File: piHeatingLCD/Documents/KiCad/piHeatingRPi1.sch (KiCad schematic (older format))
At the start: 17 parts, among them J1 Raspberry_Pi_1_all_pin_ordered, J2 10-pin_header_LCD_interface, J3 3-pin_KY-019_relay_header, J4 3_pin_Dallas_1-wire_connector, J5 2-pin_NO_switch_header, J6 2-pin_NO_switch_header, J7 2-pin_NO_switch_header, J8 2-pin_NO_switch_header

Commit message: updated kicad
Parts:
- added D1: LED, My_Misc:CP_Radial_D5.0mm_P2.50mm_larger_pads, symbol Device:LED
- added R10: R, My_Misc:R_Axial_DIN0207_L6.3mm_D2.5mm_P10.16mm_Horizontal_larger_pads, symbol Device:R
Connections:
- net at J1.8 (GPIO14/TXD), R1.2: now also J4.2 (DQ); no longer J3.1 (S)
- net at J1.1 (3V3), J2.9 (LED+), J5.1 (+)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: no longer J3.2 (Vcc), R1.1
- net at J1.25 (GND), J2.1 (VSS), J3.3 (GND)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: now also R10.2
- net at J1.10 (GPIO15/RXD): now also J3.1 (S), D1.2 (A); no longer J4.2 (DQ)
- net at J1.2 (5V), J2.2 (VDD), J4.3 (Vdd): now also J3.2 (Vcc), R1.1
- new net: D1.1 (K), R10.1
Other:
- moved on the sheet: J3, J4, R1
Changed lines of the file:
@@
 L My_Headers:3-pin_KY-019_relay_header J3
 U 1 1 5E585F50
-P 9800 2250
-F 0 "J3" H 9969 2265 50  0000 L CNN
-F 1 "3-pin_KY-019_relay_header" H 9800 2050 50  0001 C CNN
-F 2 "My_Headers:3-pin_KY-019_Relay_header_larger_pads" H 9800 2250 50  0001 C CNN
-F 3 "~" H 9800 2250 50  0001 C CNN
-	1    9800 2250
+P 9750 2550
+F 0 "J3" H 9919 2565 50  0000 L CNN
+F 1 "3-pin_KY-019_relay_header" H 9750 2350 50  0000 C CNN
+F 2 "My_Headers:3-pin_KY-019_Relay_header_larger_pads" H 9750 2550 50  0001 C CNN
+F 3 "~" H 9750 2550 50  0001 C CNN
+	1    9750 2550
 	1    0    0    -1
 $EndComp
@@
 L My_Headers:3_pin_Dallas_1-wire_connector J4
 U 1 1 5E58672E
-P 9800 2650
-F 0 "J4" H 9969 2665 50  0000 L CNN
-F 1 "3_pin_Dallas_1-wire_connector" H 9800 2450 50  0001 C CNN
-F 2 "My_Headers:3_pin_Dallas_1-wire_header_larger_pads" H 9800 2650 50  0001 C CNN
-F 3 "~" H 9800 2650 50  0001 C CNN
-	1    9800 2650
-	1    0    0    -1
-$EndComp
-$Comp
-L Device:R R1
-U 1 1 5E5AAFEA
-P 9000 2150
-F 0 "R1" H 9070 2196 50  0000 L CNN
-F 1 "4.7k" H 9070 2105 50  0000 L CNN
-F 2 "My_Misc:R_Axial_DIN0207_L6.3mm_D2.5mm_P10.16mm_Horizontal_larger_pads" V 8930 2150 50  0001 C CNN
-F 3 "~" H 9000 2150 50  0001 C CNN
-	1    9000 2150
-	0    -1   -1   0
+P 9750 2050
+F 0 "J4" H 9919 2065 50  0000 L CNN
+F 1 "3_pin_Dallas_1-wire_connector" H 9750 1850 50  0000 C CNN
+F 2 "My_Headers:3_pin_Dallas_1-wire_header_larger_pads" H 9750 2050 50  0001 C CNN
+F 3 "~" H 9750 2050 50  0001 C CNN
+	1    9750 2050
+	1    0    0    -1
 $EndComp
 $Comp
@@
 Connection ~ 8300 2250
 Wire Wire Line
-	9600 2550 9450 2550
-Wire Wire Line
-	8300 2750 8300 2250
-Wire Wire Line
-	8300 2750 9600 2750
-Wire Wire Line
 	9050 3350 8850 3350
 Wire Wire Line
@@
 Connection ~ 10450 3550
 Wire Wire Line
-	9450 2550 9450 2900
-Wire Wire Line
 	10450 2900 10450 3250
 Connection ~ 10450 3250
 Wire Wire Line
-	9600 2350 9450 2350
-Wire Wire Line
 	4000 1600 4000 3450
 Connection ~ 4000 3450
 Wire Wire Line
 	4000 3450 3400 3450
-Wire Wire Line
-	9150 2150 9350 2150
-Wire Wire Line
-	9350 2550 9350 2150
-Connection ~ 9350 2150
-Wire Wire Line
-	9350 2150 9600 2150
-Wire Wire Line
-	9450 2550 9450 2350
-Connection ~ 9450 2550
 $Comp
 L My_RaspberryPi:Raspberry_Pi_1_all_pin_ordered J1
@@
 	1    0    0    -1
 $EndComp
-Connection ~ 9450 2900
-Wire Wire Line
-	9450 2900 10450 2900
 Wire Wire Line
 	4000 1600 8200 1600
@@
 	6200 2250 8300 2250
 Wire Wire Line
-	6200 2550 9350 2550
-Wire Wire Line
-	6200 2650 9600 2650
-Wire Wire Line
-	8200 2900 9450 2900
-Wire Wire Line
 	3800 2250 3800 1700
 Wire Wire Line
 	3800 1700 8100 1700
-Wire Wire Line
-	8100 1700 8100 2150
 Wire Wire Line
 	8100 3050 8850 3050
@@
 	3600 1500 8300 1500
 Wire Wire Line
-	8300 1500 8300 2250
-Wire Wire Line
-	8850 2150 8600 2150
-Connection ~ 8100 2150
-Wire Wire Line
-	8100 2150 8100 3050
-Wire Wire Line
-	9600 2250 8600 2250
-Wire Wire Line
-	8600 2250 8600 2150
-Connection ~ 8600 2150
-Wire Wire Line
-	8600 2150 8100 2150
-Wire Wire Line
-	8200 1600 8200 2900
+	8300 1500 8300 1750
+Wire Wire Line
+	8200 1600 8200 1950
+$Comp
+L Device:LED D1
+U 1 1 5E673B9E
+P 9800 1500
+F 0 "D1" H 9793 1245 50  0000 C CNN
+F 1 "LED" H 9793 1336 50  0000 C CNN
+F 2 "My_Misc:CP_Radial_D5.0mm_P2.50mm_larger_pads" H 9800 1500 50  0001 C CNN
+F 3 "~" H 9800 1500 50  0001 C CNN
+	1    9800 1500
+	-1   0    0    1
+$EndComp
+$Comp
+L Device:R R10
+U 1 1 5E67419A
+P 9800 1000
+F 0 "R10" V 9593 1000 50  0000 C CNN
+F 1 "R" V 9684 1000 50  0000 C CNN
+F 2 "My_Misc:R_Axial_DIN0207_L6.3mm_D2.5mm_P10.16mm_Horizontal_larger_pads" V 9730 1000 50  0001 C CNN
+F 3 "~" H 9800 1000 50  0001 C CNN
+	1    9800 1000
+	0    1    1    0
+$EndComp
+$Comp
+L Device:R R1
+U 1 1 5E5AAFEA
+P 8950 1750
+F 0 "R1" H 9020 1796 50  0000 L CNN
+F 1 "4.7k" H 9020 1705 50  0000 L CNN
+F 2 "My_Misc:R_Axial_DIN0207_L6.3mm_D2.5mm_P10.16mm_Horizontal_larger_pads" V 8880 1750 50  0001 C CNN
+F 3 "~" H 8950 1750 50  0001 C CNN
+	1    8950 1750
+	0    -1   -1   0
+$EndComp
+Wire Wire Line
+	8200 2900 10450 2900
+Wire Wire Line
+	8100 1700 8100 3050
+Wire Wire Line
+	9550 2150 8300 2150
+Connection ~ 8300 2150
+Wire Wire Line
+	8300 2150 8300 2250
+Wire Wire Line
+	8800 1750 8300 1750
+Connection ~ 8300 1750
+Wire Wire Line
+	8300 1750 8300 2150
+Wire Wire Line
+	9100 1750 9300 1750
+Wire Wire Line
+	9300 1750 9300 2050
+Wire Wire Line
+	9300 2050 9550 2050
+Wire Wire Line
+	9550 1950 8200 1950
+Connection ~ 8200 1950
+Wire Wire Line
+	8200 1950 8200 2650
+Wire Wire Line
+	9550 2550 8300 2550
+Wire Wire Line
+	8300 2550 8300 2250
+Wire Wire Line
+	9550 2650 8200 2650
+Connection ~ 8200 2650
+Wire Wire Line
+	8200 2650 8200 2900
+Wire Wire Line
+	9300 2050 7250 2050
+Wire Wire Line
+	7250 2050 7250 2550
+Wire Wire Line
+	7250 2550 6200 2550
+Connection ~ 9300 2050
+Wire Wire Line
+	9550 2450 9400 2450
+Wire Wire Line
+	7350 2450 7350 2650
+Wire Wire Line
+	7350 2650 6200 2650
+Wire Wire Line
+	9400 2450 9400 1500
+Wire Wire Line
+	9400 1500 9650 1500
+Connection ~ 9400 2450
+Wire Wire Line
+	9400 2450 7350 2450
+Wire Wire Line
+	9950 1500 10250 1500
+Wire Wire Line
+	10250 1500 10250 1000
+Wire Wire Line
+	10250 1000 9950 1000
+Wire Wire Line
+	9650 1000 8200 1000
+Wire Wire Line
+	8200 1000 8200 1600
+Connection ~ 8200 1600
 $EndSCHEMATC

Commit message: added resistor value in kicad
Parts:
- R10: value R -> 120R
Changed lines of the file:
@@
 P 9800 1000
 F 0 "R10" V 9593 1000 50  0000 C CNN
-F 1 "R" V 9684 1000 50  0000 C CNN
+F 1 "120R" V 9684 1000 50  0000 C CNN
 F 2 "My_Misc:R_Axial_DIN0207_L6.3mm_D2.5mm_P10.16mm_Horizontal_larger_pads" V 9730 1000 50  0001 C CNN
 F 3 "~" H 9800 1000 50  0001 C CNN

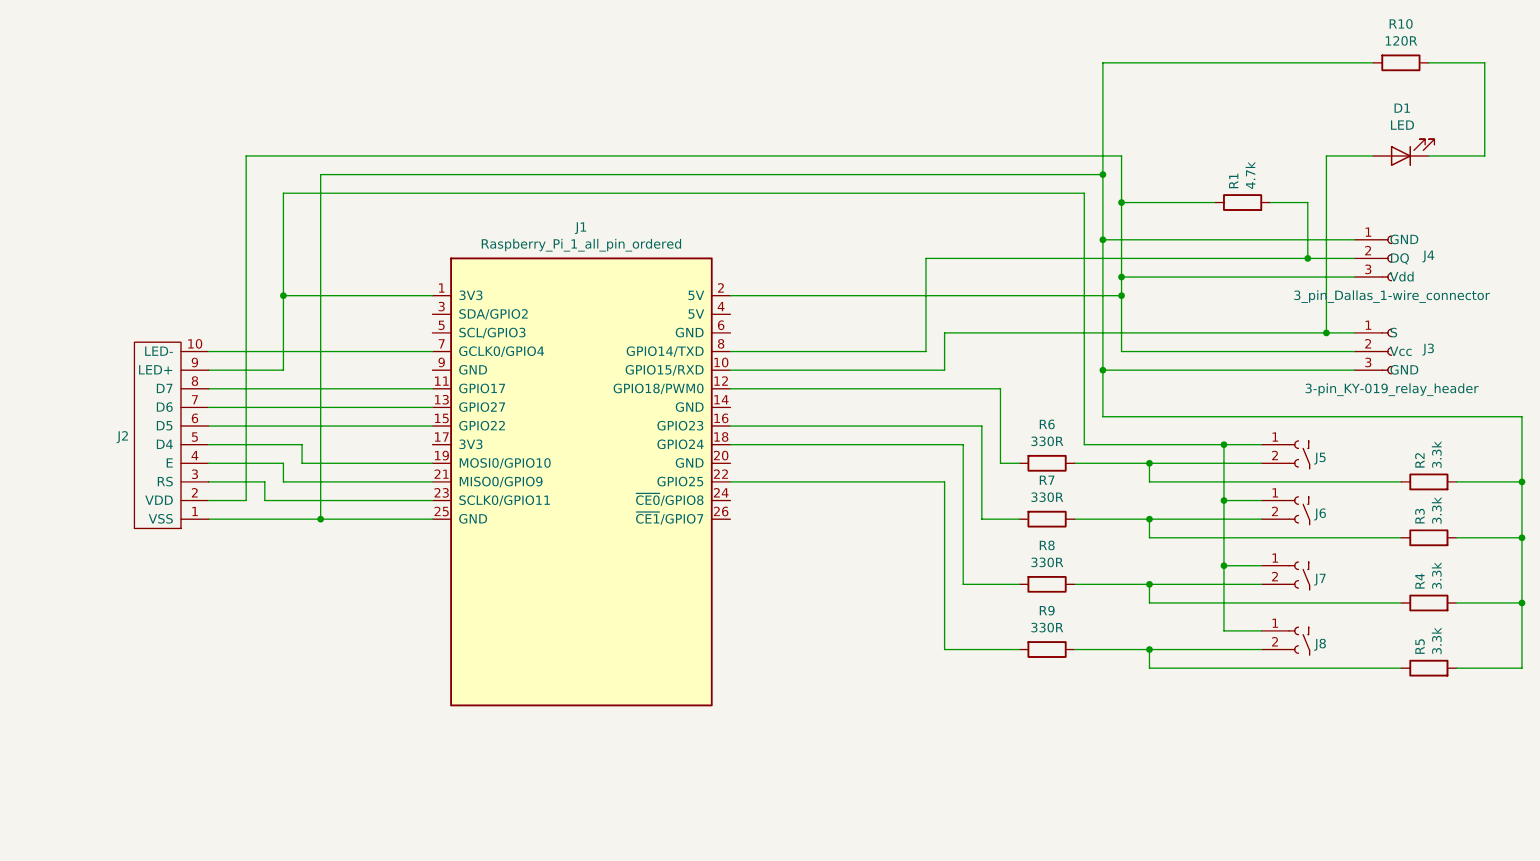
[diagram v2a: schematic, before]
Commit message: moved dallas from 5V to 3.3V
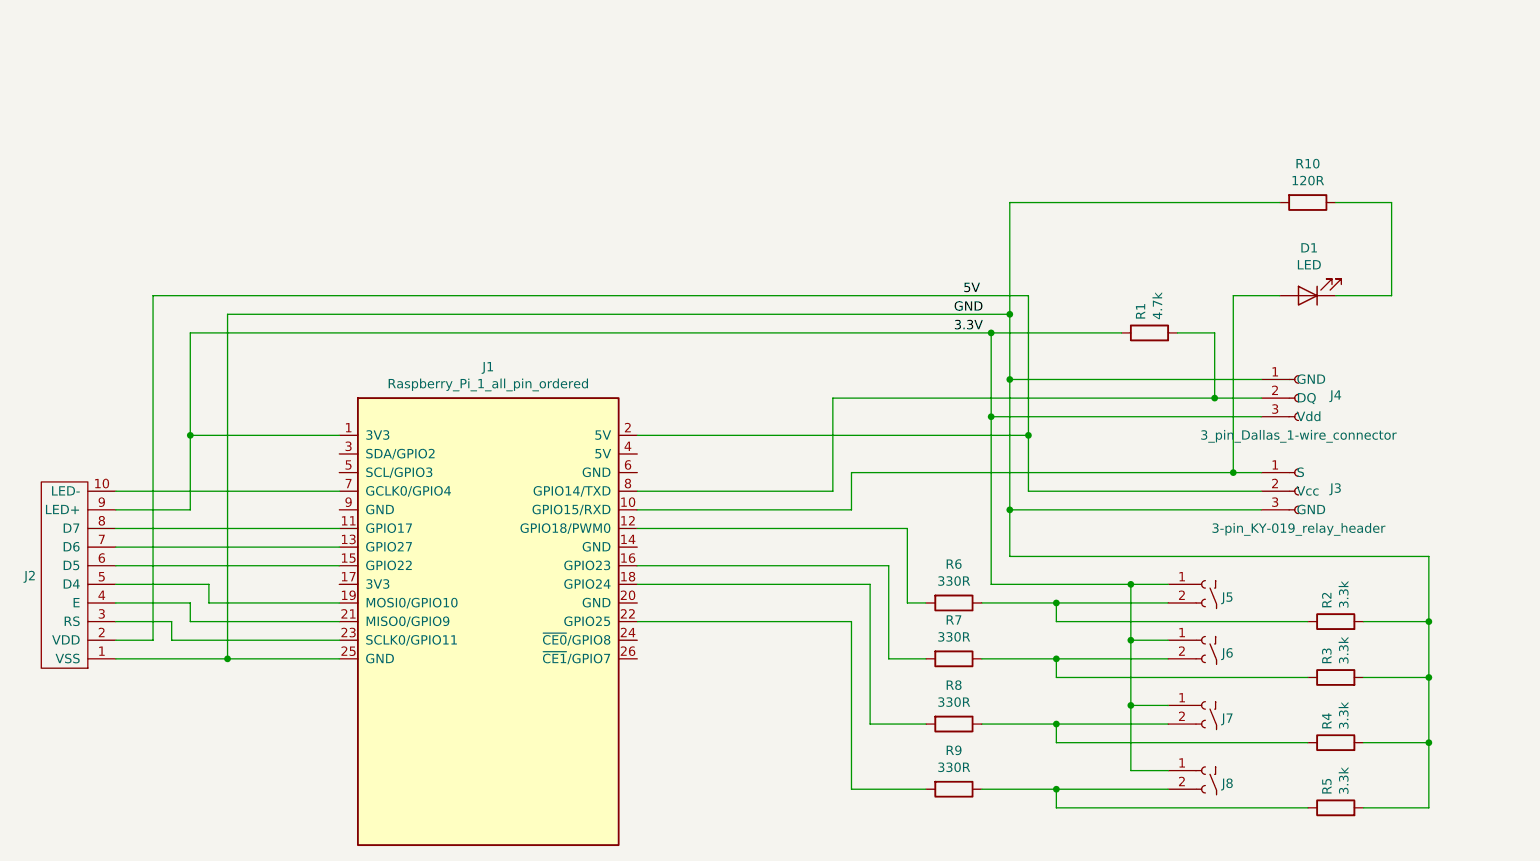
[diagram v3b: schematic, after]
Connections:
- net 5V: now reaches J1.2 (5V), J2.2 (VDD), J3.2 (Vcc)
- net 5V: no longer J4.3 (Vdd), R1.1
- net GND: now reaches J1.25 (GND), J2.1 (VSS), J3.3 (GND), J4.1 (GND), R10.2, R2.2, R3.2, R4.2, R5.2
- net 3.3V: now reaches J1.1 (3V3), J2.9 (LED+), J5.1 (+), J6.1 (+), J7.1 (+), J8.1 (+)
- net 3.3V: now also J4.3 (Vdd), R1.1
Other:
- moved on the sheet: D1, J1, J2, J3, J4, J5, J6, J7, J8, R1, R10, R2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
